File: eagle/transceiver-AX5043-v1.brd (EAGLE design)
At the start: 40 x 35 mm, 33 parts, among them J1 2X8X1.27, J4 U.FL, J5 U.FL, J6 U.FL, U1 U-ONSEMI-AX5043, U2 LP2985XX-N, X1 TAITIEN-TY

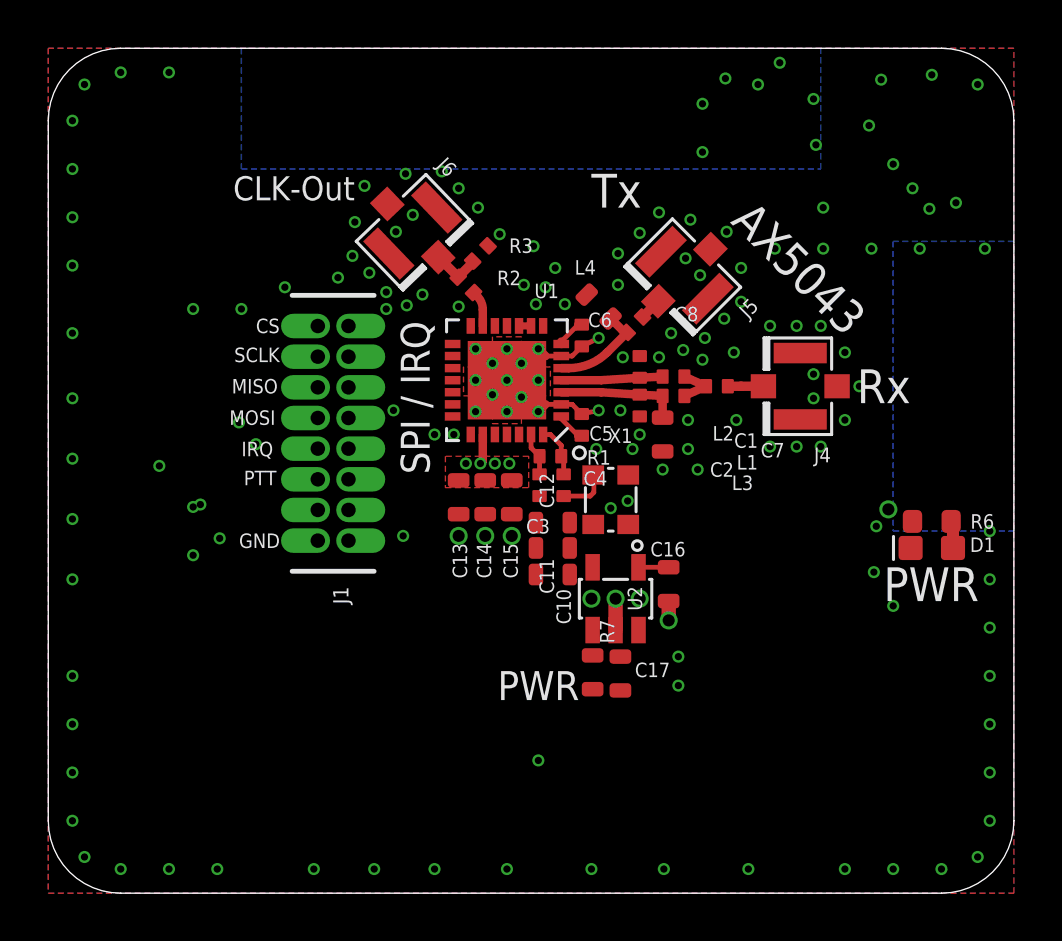
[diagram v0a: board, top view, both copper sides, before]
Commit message: Added the modified AX5043 transceiver block and some datasheets
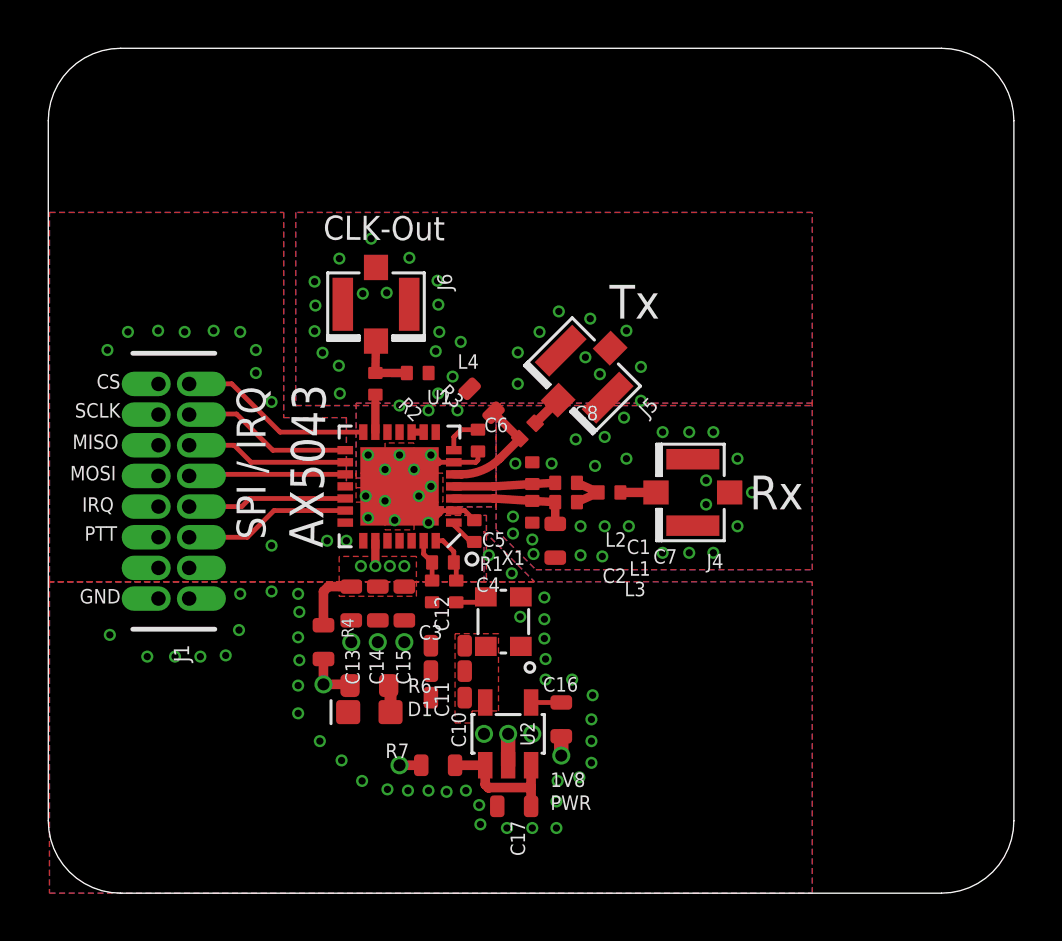
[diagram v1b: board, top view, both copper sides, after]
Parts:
- added R4: 0, oresat-rcl:.0603-C-NOSILK
- J1: value 2X8X1.27 -> HARWIN-2X8X1.27; device J-2X8X1.27:2X8X1.27 -> J-Harwin-M50-3610842R-2X8X1.27_Male :2X8X1.27
- moved D1 24.3 mm to (45.3, -11.3)
- moved R6 24.3 mm to (45.3, -10.2)
- moved R7 7.47 mm to (48.1, -13.5), turned to 180 degrees
- moved C16 7.15 mm to (53.2, -11.6)
- moved U2 7.15 mm to (51.0, -12.2)
- moved C17 7.04 mm to (51.3, -15.2), turned to 180 degrees
- moved J1 7.02 mm to (37.2, -2.15)
- moved X1 6.73 mm to (50.9, -7.55)
- moved C10 6.70 mm to (48.5, -10.7)
- moved C11 6.70 mm to (48.5, -9.60)
- moved C12 6.70 mm to (48.5, -8.55)
- moved C13 6.26 mm to (44.5, -6.80)
- moved C14 6.26 mm to (45.6, -6.80)
- moved C15 6.26 mm to (46.8, -6.80)
- moved C2 6.26 mm to (52.0, -3.00)
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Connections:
- removed net 2V7: C13.1, C14.1, C15.1, C17.1, R6.1, R7.1, R7.2, U1.23, U2.1, U2.3
- new net 3.3V: C13.1, C14.1, C15.1, C17.1, R4.1, R4.2, R6.1, R7.1, R7.2, U1.23, U2.1, U2.3
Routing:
- net 3.3V: track 0.00 -> 49.0 mm, vias 0 -> 6
- net 2V7: track 32.7 -> 0.00 mm, vias 5 -> 0
- net CS: track 0.00 -> 8.05 mm
- net SCLK: track 0.00 -> 7.10 mm
- net PWRAMP: track 0.00 -> 6.92 mm
- net MISO: track 0.00 -> 6.76 mm
- net IRQ: track 0.00 -> 6.60 mm
- net MOSI: track 0.00 -> 6.49 mm
- net GND: track 7.78 -> 6.84 mm, vias 164 -> 132
- net N$6: track 2.05 -> 1.40 mm
- net ANTP1: track 4.13 -> 4.74 mm
- net REF-OUT: track 2.09 -> 2.64 mm
- added copper zone on layer 1, net 1V8
- added copper zone on layer 1, net 3.3V
- removed copper zone on layer 1, net 2V7
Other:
- board text added: "1V8"
- board text removed: "400 - 525 MHz 800 - 1050 MHz"
- board text removed: "Transceiver - AX5043 PSAS / OreSat 2019-10-18 v1.0 E.M. KJ7AOG"

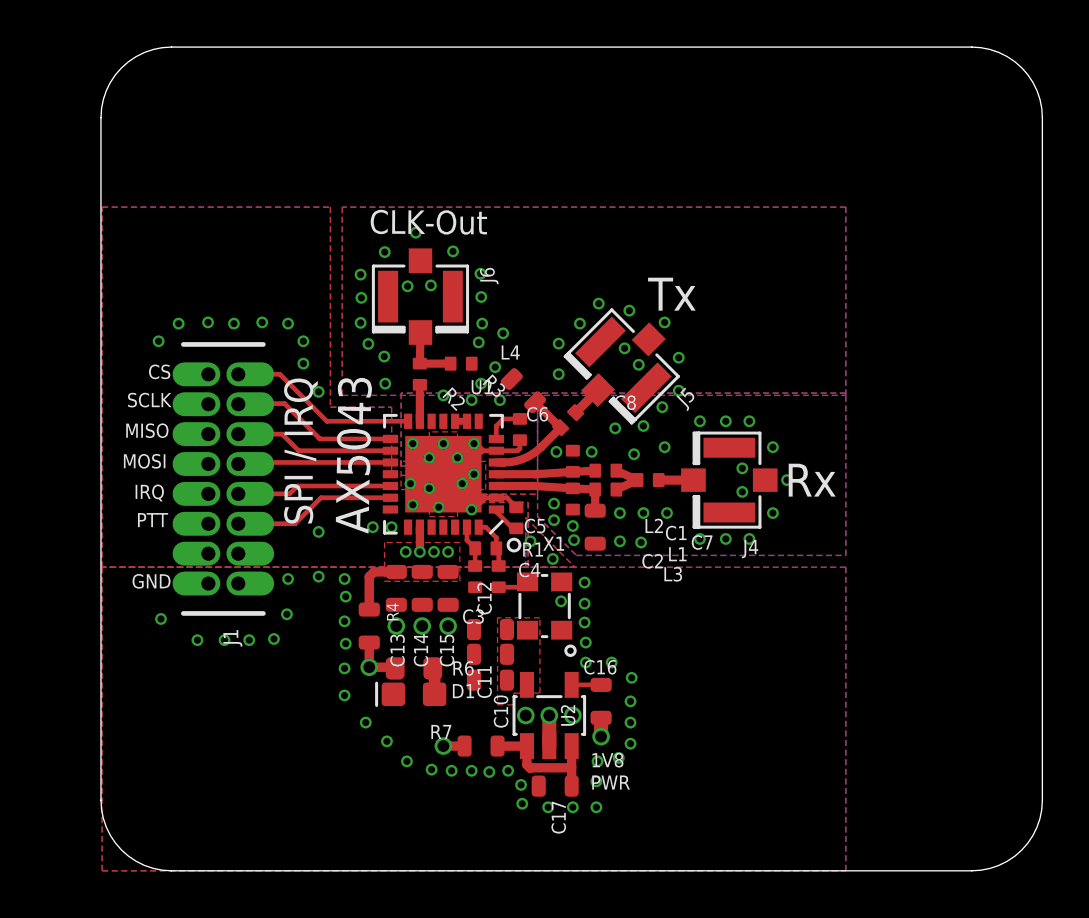
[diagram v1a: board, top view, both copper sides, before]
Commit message: integrated 2 AX5043 radios and connected up the eMMC
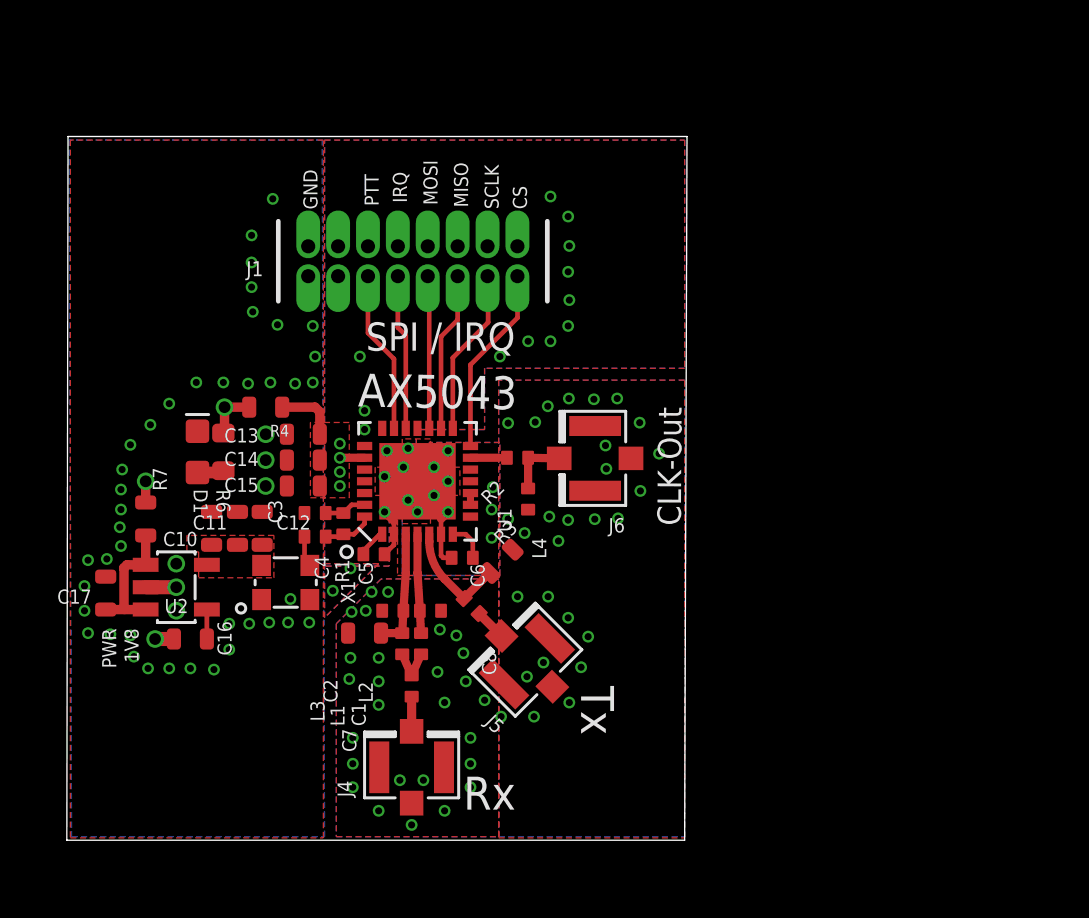
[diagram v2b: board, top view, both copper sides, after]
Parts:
- moved C17 20.8 mm to (32.2, -7.00), turned to 90 degrees
- moved J4 18.2 mm to (45.2, -14.4), turned to 90 degrees
- moved C16 17.7 mm to (35.8, -8.95), turned to 180 degrees
- moved R7 17.2 mm to (33.9, -3.85), turned to 90 degrees
- moved U2 16.8 mm to (35.2, -6.75), turned to 0 degrees
- moved D1 13.8 mm to (36.1, -1.00), turned to 90 degrees
- moved C10 13.5 mm to (36.7, -4.25), turned to 90 degrees
- moved C7 13.3 mm to (45.2, -10.9), turned to 90 degrees
- moved J5 13.3 mm to (50.1, -9.90), turned to 135 degrees
- moved J1 12.3 mm to (45.2, 7.10), turned to 180 degrees
- moved R6 12.3 mm to (37.2, -1.00), turned to 270 degrees
- moved C11 12.0 mm to (37.8, -4.25), turned to 90 degrees
- moved X1 11.0 mm to (39.9, -6.55), turned to 0 degrees
- moved L1 10.9 mm to (44.8, -9.15), turned to 90 degrees
- moved L3 10.8 mm to (43.2, -8.70), turned to 180 degrees
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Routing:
- net 3.3V: track 49.0 -> 17.5 mm
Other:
- board size 40 x 35 mm -> 26.3 x 29.9 mm

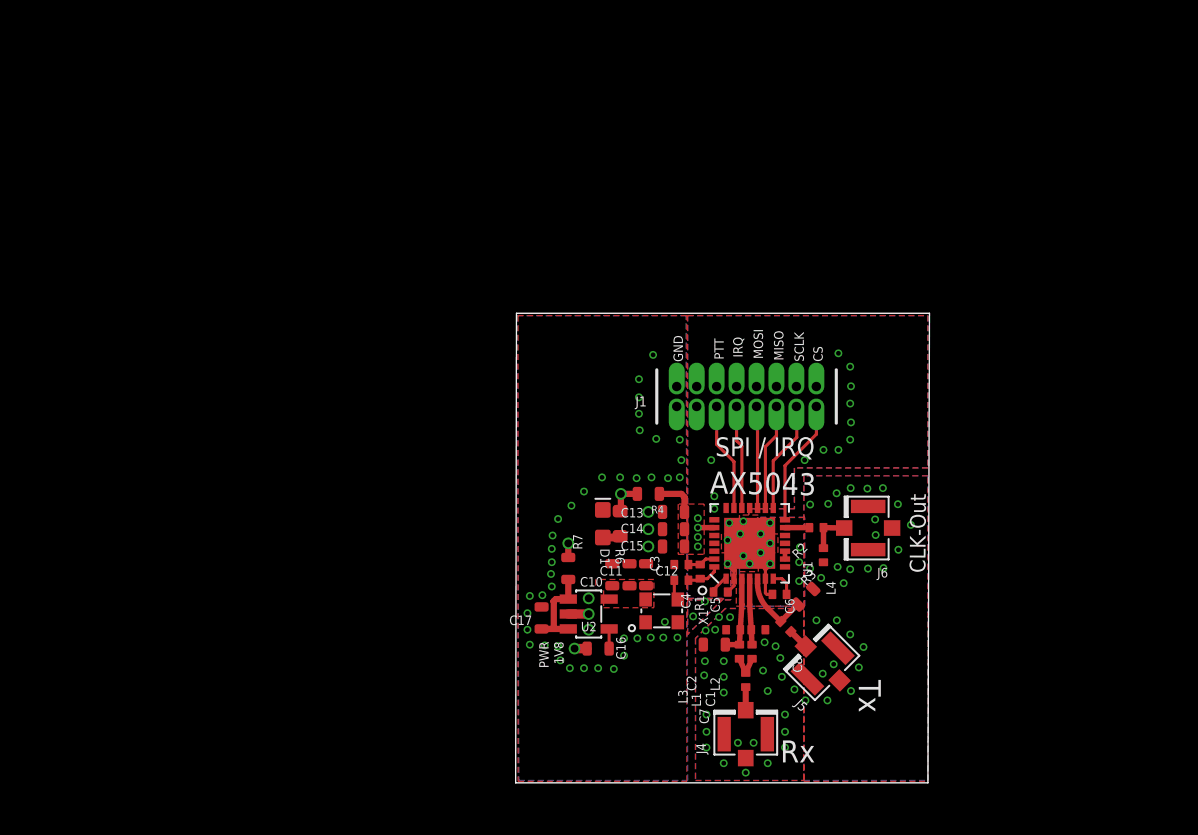
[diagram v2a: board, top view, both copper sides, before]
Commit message: put in segregated ground planes, added the version of the project proposal that was signed to the docs folder
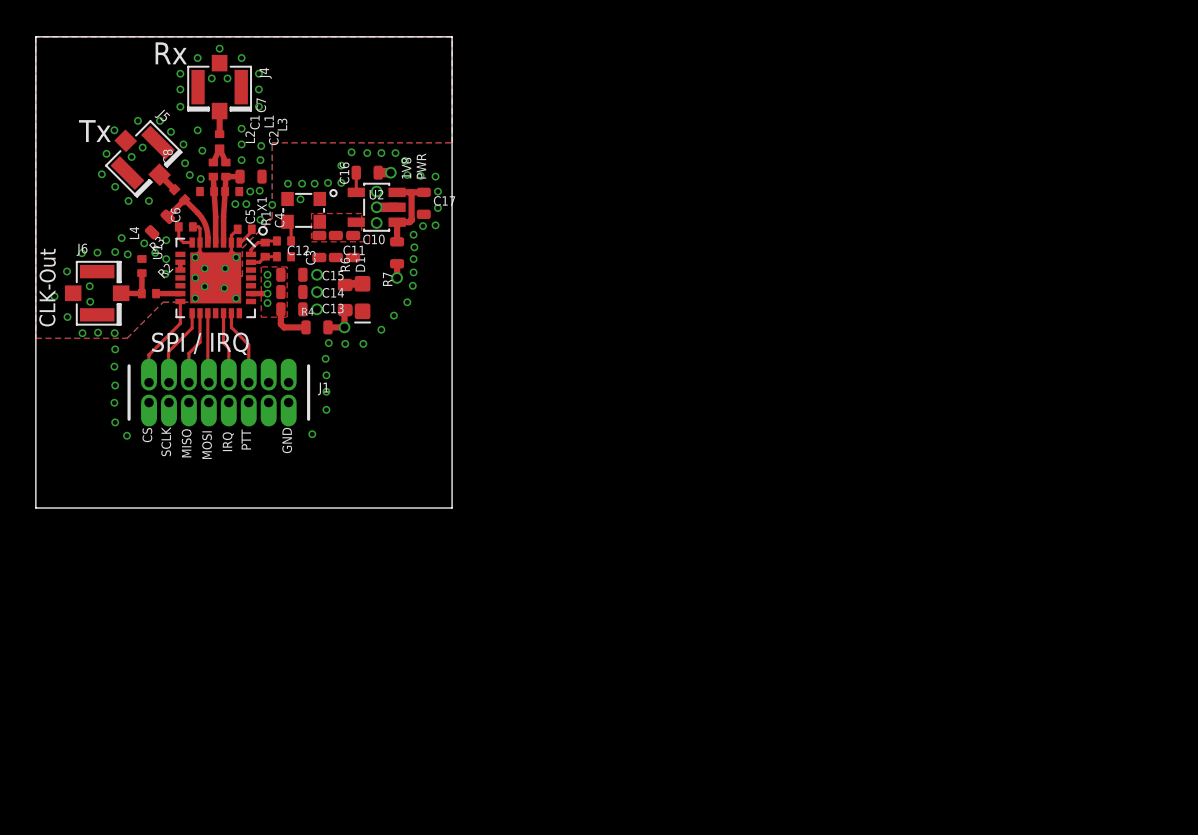
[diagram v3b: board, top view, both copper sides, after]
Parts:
- moved J5 54.0 mm to (6.80, 22.3), turned to 315 degrees
- moved J4 53.1 mm to (11.7, 26.8), turned to 270 degrees
- moved J6 51.3 mm to (3.90, 13.7), turned to 0 degrees
- moved C7 47.9 mm to (11.7, 23.4), turned to 270 degrees
- moved L4 47.4 mm to (7.90, 18.1), turned to 45 degrees
- moved C8 47.4 mm to (9.15, 19.9), turned to 315 degrees
- moved R3 47.1 mm to (6.75, 15.4), turned to 90 degrees
- moved C1 46.0 mm to (11.3, 21.6), turned to 270 degrees
- moved R2 45.0 mm to (7.20, 13.7), turned to 180 degrees
- moved L1 44.9 mm to (12.1, 21.6), turned to 270 degrees
- moved L2 44.8 mm to (10.9, 20.1), turned to 0 degrees
- moved C6 44.5 mm to (9.55, 17.9), turned to 180 degrees
- moved C2 42.4 mm to (12.5, 20.1), turned to 180 degrees
- moved L3 41.9 mm to (13.7, 21.1), turned to 0 degrees
- moved C5 38.1 mm to (13.3, 17.8), turned to 180 degrees
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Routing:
- net SCLK: track 7.10 -> 5.05 mm
- net CS: track 8.05 -> 6.00 mm
- net PWRAMP: track 6.92 -> 4.87 mm
- net MOSI: track 6.49 -> 4.44 mm
- net IRQ: track 6.60 -> 4.55 mm
- net MISO: track 6.76 -> 4.71 mm
- net GND: track 6.70 -> 6.67 mm, vias 132 -> 114
- added copper zone on layer 15, net GND1
- added copper zone on layer 16, net GND1
- added copper zone on layer 2, net GND1
- removed copper zone on layer 15, net GND
- removed copper zone on layer 16, net GND
- removed copper zone on layer 2, net GND
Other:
- board size 26.3 x 29.9 mm -> 26.5 x 30 mm
- board text removed: "AX5043"
